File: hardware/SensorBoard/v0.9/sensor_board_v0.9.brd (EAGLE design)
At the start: 52.5 x 43 mm, 43 parts, among them IC1 BMP280, IC2 VREF, J3 USB-MICROB, U1 LMP91000, U10 CCS811, U11 RFM69HW, U2 TSL2561, U3 ATMEGA328P-MU, U7 SHT31, U8 MCP1703/3.3V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

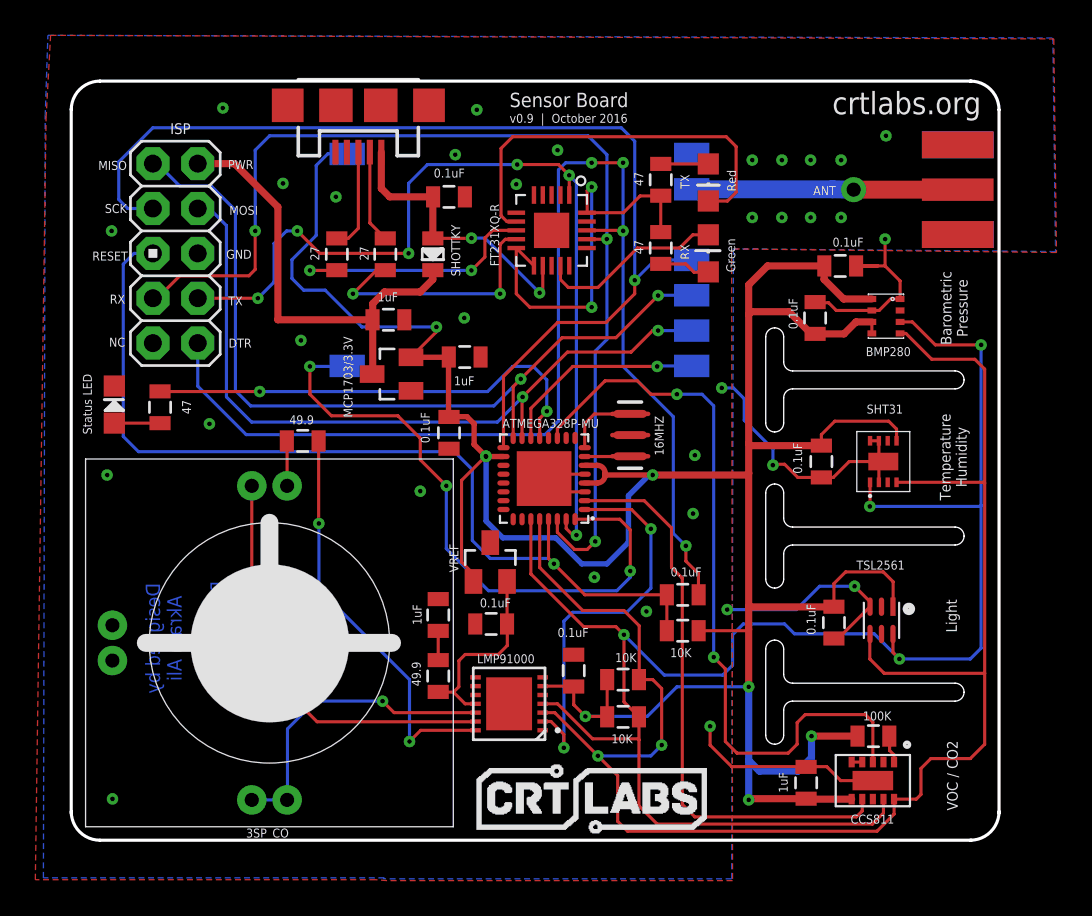
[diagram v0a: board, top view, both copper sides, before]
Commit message: Rearranged several compoents around LMP91000
Rerouted several traces, other touch ups
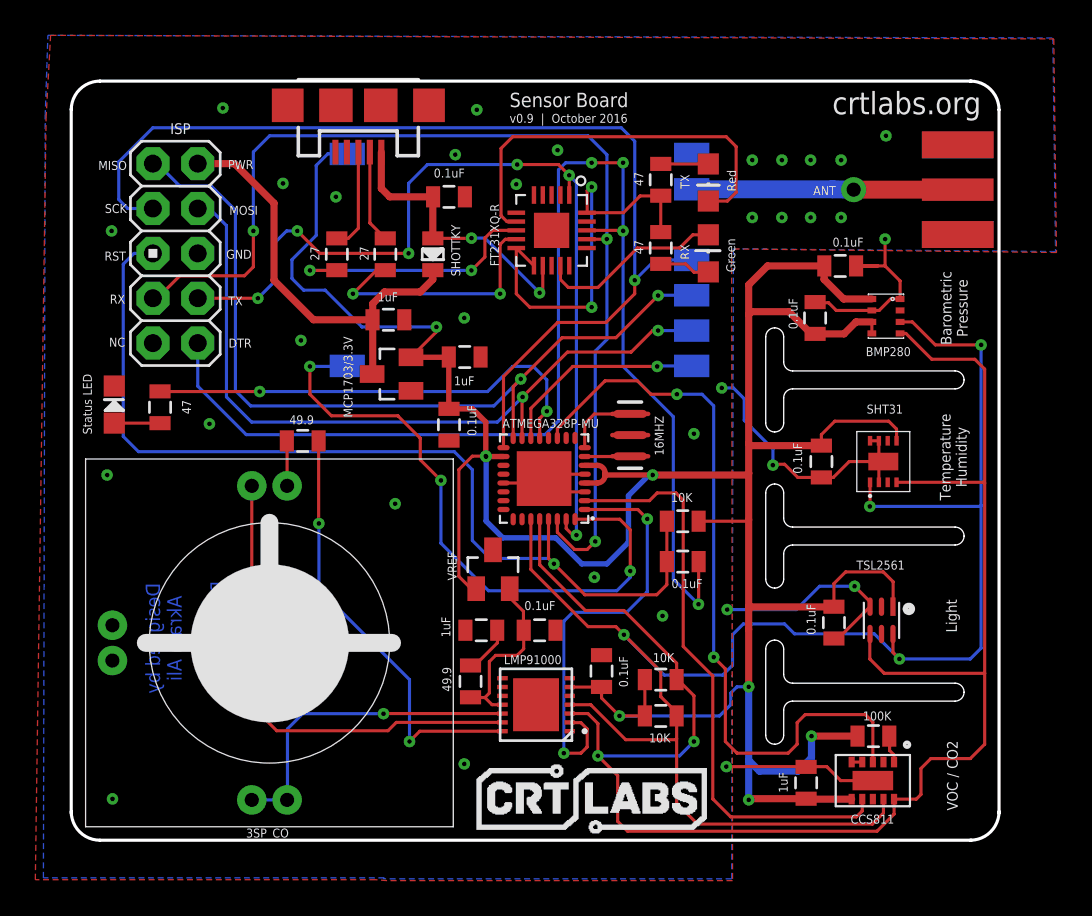
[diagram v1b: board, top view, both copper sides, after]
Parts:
- moved R13 6.20 mm to (38.0, 24.0)
- moved C10 2.77 mm to (29.9, 17.8), turned to 0 degrees
- moved C9 2.59 mm to (26.6, 17.8), turned to 180 degrees
- moved R5 2.13 mm to (36.8, 13.0)
- moved R6 2.13 mm to (36.8, 15.0)
- moved C12 1.88 mm to (38.0, 21.7)
- moved R3 1.85 mm to (26.0, 14.9)
- moved C7 1.58 mm to (33.4, 15.5)
- moved U1 1.52 mm to (29.7, 13.6)
- moved C15 0.46 mm to (24.8, 29.5)
- moved IC2 0.43 mm to (27.3, 21.3)
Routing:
- net RE: track 23.9 -> 27.4 mm
- net DTR: track 70.7 -> 73.6 mm
- net RESET: track 53.2 -> 55.0 mm
- net MENB: track 22.7 -> 24.4 mm
- net N$9: track 23.2 -> 24.7 mm
- net SCL: track 94.2 -> 95.7 mm
- net PWR: track 25.8 -> 24.6 mm
- net N$10: track 1.65 -> 2.77 mm
- net WE: track 17.6 -> 18.6 mm
- net SDA: track 97.5 -> 96.6 mm
- net VREF: track 11.0 -> 10.2 mm
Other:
- board text added: "RST"
- board text removed: "RESET"

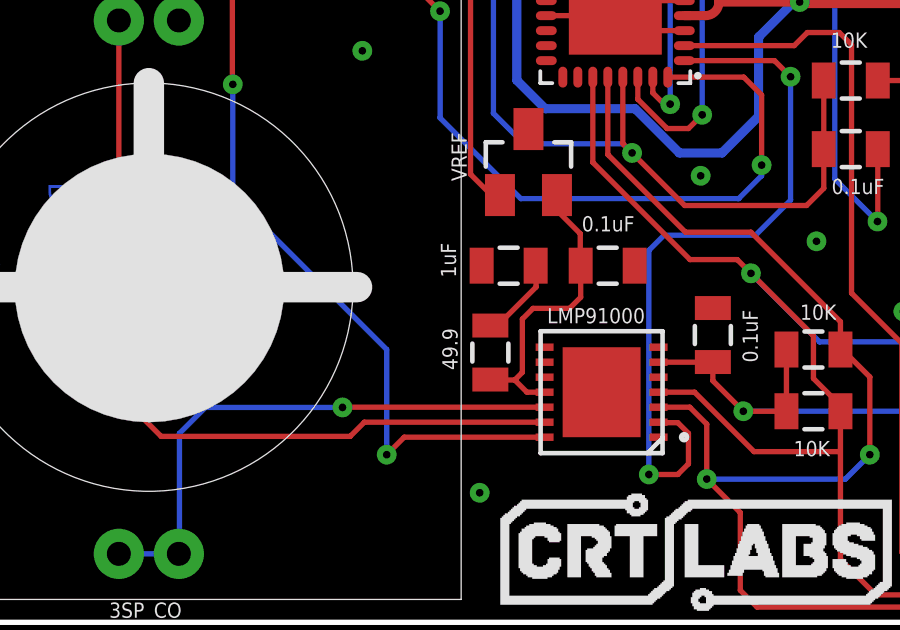
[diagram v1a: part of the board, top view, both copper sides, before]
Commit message: Corrected resistor and capacitor values for voltage ref.
Also added adjusted CCS811 tstop pads
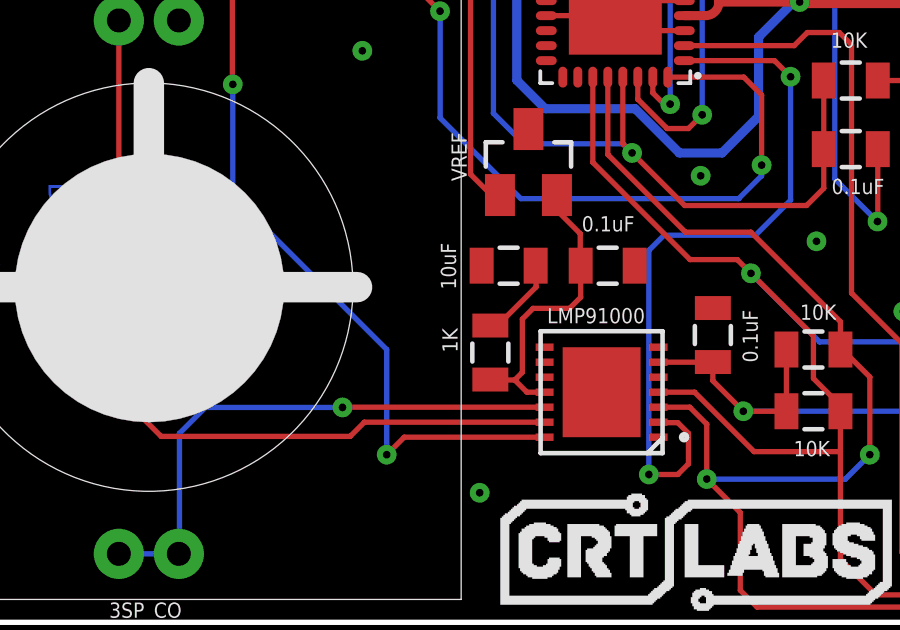
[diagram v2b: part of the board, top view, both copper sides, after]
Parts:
- C9: value 1uF -> 10uF
- R3: value 49.9 -> 1K
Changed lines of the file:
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@@
 <?xml version="1.0" encoding="utf-8"?>
 <!DOCTYPE eagle SYSTEM "eagle.dtd">
-<eagle version="7.6.0">
+<eagle version="7.7.0">
 <drawing>
 <settings>
@@
 <layers>
 <layer number="1" name="Top" color="4" fill="1" visible="yes" active="yes"/>
+<layer number="2" name="Route2" color="1" fill="3" visible="no" active="yes"/>
+<layer number="3" name="Route3" color="4" fill="3" visible="no" active="yes"/>
+<layer number="4" name="Route4" color="1" fill="4" visible="no" active="yes"/>
+<layer number="5" name="Route5" color="4" fill="4" visible="no" active="yes"/>
+<layer number="6" name="Route6" color="1" fill="8" visible="no" active="yes"/>
+<layer number="7" name="Route7" color="4" fill="8" visible="no" active="yes"/>
+<layer number="8" name="Route8" color="1" fill="2" visible="no" active="yes"/>
+<layer number="9" name="Route9" color="4" fill="2" visible="no" active="yes"/>
+<layer number="10" name="Route10" color="1" fill="7" visible="no" active="yes"/>
+<layer number="11" name="Route11" color="4" fill="7" visible="no" active="yes"/>
+<layer number="12" name="Route12" color="1" fill="5" visible="no" active="yes"/>
+<layer number="13" name="Route13" color="4" fill="5" visible="no" active="yes"/>
+<layer number="14" name="Route14" color="1" fill="6" visible="no" active="yes"/>
+<layer number="15" name="Route15" color="4" fill="6" visible="no" active="yes"/>
 <layer number="16" name="Bottom" color="1" fill="1" visible="yes" active="yes"/>
 <layer number="17" name="Pads" color="2" fill="1" visible="yes" active="yes"/>
@@
 <layer number="27" name="tValues" color="7" fill="1" visible="yes" active="yes"/>
 <layer number="28" name="bValues" color="7" fill="1" visible="yes" active="yes"/>
-<layer number="29" name="tStop" color="7" fill="3" visible="no" active="yes"/>
+<layer number="29" name="tStop" color="7" fill="3" visible="yes" active="yes"/>
 <layer number="30" name="bStop" color="7" fill="6" visible="no" active="yes"/>
 <layer number="31" name="tCream" color="7" fill="4" visible="no" active="yes"/>
@@
 <attribute name="VALUE" x="29.0576" y="18.9738" size="0.508" layer="121" font="vector"/>
 </element>
-<element name="R3" library="SparkFun-Passives" package="0805" value="49.9" x="26.0096" y="14.9352" smashed="yes" rot="R270">
+<element name="R3" library="SparkFun-Passives" package="0805" value="1K" x="26.0096" y="14.9352" smashed="yes" rot="R270">
 <attribute name="MF" value="" x="26.0096" y="14.9352" size="1.778" layer="27" rot="R270" display="off"/>
 <attribute name="MPN" value="" x="26.0096" y="14.9352" size="1.778" layer="27" rot="R270" display="off"/>
@@
 <attribute name="VALUE" x="24.4094" y="15.748" size="0.508" layer="121" font="vector" rot="R270"/>
 </element>
-<element name="C9" library="SparkFun-Passives" package="0805" value="1uF" x="26.6192" y="17.8308" smashed="yes" rot="R180">
+<element name="C9" library="SparkFun-Passives" package="0805" value="10uF" x="26.6192" y="17.8308" smashed="yes" rot="R180">
 <attribute name="VALUE" x="24.3586" y="18.5928" size="0.508" layer="121" font="vector" rot="R270"/>
 </element>

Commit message: updated LED descriptions
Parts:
- renumbered LED2 to LED1
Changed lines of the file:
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@@
 </element>
 <element name="C3" library="SparkFun-Passives" package="0805" value="0.1uF" x="46.5836" y="18.2626" smashed="yes" rot="R270">
-<attribute name="MPN" value="CC0603KRX7R7BB104" x="46.5836" y="18.2626" size="1.778" layer="27" rot="R270" display="off"/>
+<attribute name="MPN" value="AC0805KRX7R9BB104" x="46.5836" y="18.2626" size="1.778" layer="27" rot="R270" display="off"/>
 <attribute name="VALUE" x="45.0342" y="19.3294" size="0.508" layer="121" font="vector" rot="R270"/>
 </element>
 <element name="C4" library="SparkFun-Passives" package="0805" value="0.1uF" x="45.8724" y="27.3812" smashed="yes" rot="R270">
-<attribute name="MPN" value="CC0603KRX7R7BB104" x="45.8724" y="27.3812" size="1.778" layer="27" rot="R270" display="off"/>
+<attribute name="MPN" value="AC0805KRX7R9BB104" x="45.8724" y="27.3812" size="1.778" layer="27" rot="R270" display="off"/>
 <attribute name="VALUE" x="44.2722" y="28.448" size="0.508" layer="121" font="vector" rot="R270"/>
 </element>
@@
 <attribute name="VALUE" x="36.9443" y="27.7241" size="0.508" layer="121" font="vector" rot="R90"/>
 </element>
-<element name="LED2" library="adafruit" package="CHIPLED_0805" value="" x="5.842" y="30.607" smashed="yes">
-<attribute name="MPN" value="LTST-C170TBKT" x="5.842" y="30.607" size="1.778" layer="27" display="off"/>
+<element name="LED1" library="adafruit" package="CHIPLED_0805" value="" x="5.842" y="30.607" smashed="yes">
+<attribute name="MPN" value="150080BS75000" x="5.842" y="30.607" size="1.778" layer="27" display="off"/>
 <attribute name="VALUE" x="8.382" y="29.337" size="1.27" layer="27" rot="R90"/>
 </element>
@@
 <element name="C12" library="SparkFun-Passives" package="0805" value="0.1uF" x="38.0238" y="21.717" smashed="yes" rot="R180">
 <attribute name="VALUE" x="39.1414" y="20.7264" size="0.508" layer="121" font="vector" rot="R180"/>
-<attribute name="MPN" value="CC0603KRX7R7BB104" x="38.0238" y="21.717" size="1.778" layer="27" rot="R180" display="off"/>
+<attribute name="MPN" value="AC0805KRX7R9BB104" x="38.0238" y="21.717" size="1.778" layer="27" rot="R180" display="off"/>
 </element>
 <element name="J2" library="SparkFun-Connectors" package="AVR_ICSP" value="" x="9.2964" y="39.1668" smashed="yes">
@@
 </element>
 <element name="RX" library="adafruit" package="CHIPLED_0805" value="Green" x="39.4716" y="39.1668" smashed="yes">
-<attribute name="MPN" value="LTST-C170TBKT" x="39.4716" y="39.1668" size="1.778" layer="27" display="off"/>
+<attribute name="MPN" value="LG R971-KN-1" x="39.4716" y="39.1668" size="1.778" layer="27" display="off"/>
 <attribute name="NAME" x="38.4048" y="38.8112" size="0.508" layer="121" font="vector" rot="R90"/>
 <attribute name="VALUE" x="40.9956" y="38.1" size="0.508" layer="121" font="vector" rot="R90"/>
 </element>
 <element name="TX" library="adafruit" package="CHIPLED_0805" value="Red" x="39.4716" y="43.18" smashed="yes" rot="R180">
-<attribute name="MPN" value="LTST-C170TBKT" x="39.4716" y="43.18" size="1.778" layer="27" rot="R180" display="off"/>
+<attribute name="MPN" value="LH R974-LP-1" x="39.4716" y="43.18" size="1.778" layer="27" rot="R180" display="off"/>
 <attribute name="NAME" x="37.8968" y="43.6372" size="0.508" layer="121" font="vector" rot="R270"/>
 <attribute name="VALUE" x="40.5384" y="43.8912" size="0.508" layer="121" font="vector" rot="R270"/>
@@
 </element>
 <element name="C11" library="SparkFun-Capacitors" package="0805" value="0.1uF" x="24.7904" y="42.3672" smashed="yes">
-<attribute name="MPN" value="CC0603KRX7R7BB104" x="24.7904" y="42.3672" size="1.778" layer="27" display="off"/>
+<attribute name="MPN" value="AC0805KRX7R9BB104" x="24.7904" y="42.3672" size="1.778" layer="27" display="off"/>
 <attribute name="VALUE" x="23.9268" y="43.4594" size="0.508" layer="121" font="vector"/>
 </element>
@@
 <element name="C15" library="SparkFun-Passives" package="0805" value="0.1uF" x="24.7904" y="29.464" smashed="yes" rot="R270">
 <attribute name="VALUE" x="25.8318" y="30.5816" size="0.508" layer="121" font="vector" rot="R270"/>
-<attribute name="MPN" value="CC0603KRX7R7BB104" x="24.7904" y="29.464" size="1.778" layer="27" rot="R270" display="off"/>
+<attribute name="MPN" value="AC0805KRX7R9BB104" x="24.7904" y="29.464" size="1.778" layer="27" rot="R270" display="off"/>
 </element>
 <element name="U10" library="CCS811" package="LGA" value="CCS811" x="46.7868" y="10.668" smashed="yes" rot="R270">
@@
 <element name="C2" library="SparkFun-Passives" package="0805" value="0.1uF" x="45.5168" y="35.5092" smashed="yes" rot="R90">
 <attribute name="VALUE" x="44.0182" y="36.6268" size="0.508" layer="121" font="vector" rot="R270"/>
-<attribute name="MPN" value="CC0603KRX7R7BB104" x="45.5168" y="35.5092" size="1.778" layer="27" rot="R90" display="off"/>
+<attribute name="MPN" value="AC0805KRX7R9BB104" x="45.5168" y="35.5092" size="1.778" layer="27" rot="R90" display="off"/>
 </element>
 <element name="C8" library="SparkFun-Passives" package="0805" value="0.1uF" x="46.9392" y="38.4556" smashed="yes" rot="R180">
 <attribute name="VALUE" x="48.26" y="40.0558" size="0.508" layer="121" font="vector" rot="R180"/>
-<attribute name="MPN" value="CC0603KRX7R7BB104" x="46.9392" y="38.4556" size="1.778" layer="27" rot="R180" display="off"/>
+<attribute name="MPN" value="AC0805KRX7R9BB104" x="46.9392" y="38.4556" size="1.778" layer="27" rot="R180" display="off"/>
 </element>
 <element name="U3" library="ATMEGA328P-MU" package="QFN50P500X500X100-33N" value="ATMEGA328P-MU" x="30.1752" y="26.416" smashed="yes" rot="R180">
@@
 <element name="C7" library="SparkFun-Passives" package="0805" value="0.1uF" x="33.4264" y="15.5194" smashed="yes" rot="R270">
 <attribute name="VALUE" x="34.925" y="14.605" size="0.508" layer="121" font="vector" rot="R90"/>
-<attribute name="MPN" value="CC0603KRX7R7BB104" x="33.4264" y="15.5194" size="1.778" layer="27" rot="R270" display="off"/>
+<attribute name="MPN" value="AC0805KRX7R9BB104" x="33.4264" y="15.5194" size="1.778" layer="27" rot="R270" display="off"/>
 </element>
 <element name="IC2" library="linear" package="SOT23" value="VREF" x="27.2796" y="21.2852" smashed="yes">
 <attribute name="VALUE" x="25.2222" y="20.6502" size="0.508" layer="121" font="vector" rot="R90"/>
-<attribute name="MPN" value="ISL60002DIH320ZCB" x="27.2796" y="21.2852" size="1.778" layer="27" display="off"/>
+<attribute name="MPN" value="ISL60002DIH320Z-TK" x="27.2796" y="21.2852" size="1.778" layer="27" display="off"/>
 </element>
 <element name="C10" library="SparkFun-Passives" package="0805" value="0.1uF" x="29.9212" y="17.8308" smashed="yes">
 <attribute name="VALUE" x="29.0576" y="18.9738" size="0.508" layer="121" font="vector"/>
-<attribute name="MPN" value="CC0603KRX7R7BB104" x="29.9212" y="17.8308" size="1.778" layer="27" display="off"/>
+<attribute name="MPN" value="AC0805KRX7R9BB104" x="29.9212" y="17.8308" size="1.778" layer="27" display="off"/>
 </element>
 <element name="R3" library="SparkFun-Passives" package="0805" value="1K" x="26.0096" y="14.9352" smashed="yes" rot="R270">
@@
 <contactref element="C6" pad="2"/>
 <contactref element="J2" pad="6"/>
-<contactref element="LED2" pad="C"/>
+<contactref element="LED1" pad="C"/>
 <contactref element="C11" pad="2"/>
 <contactref element="J3" pad="MT1"/>
@@
 <signal name="N$3">
 <contactref element="R4" pad="2"/>
-<contactref element="LED2" pad="A"/>
+<contactref element="LED1" pad="A"/>
 <wire x1="8.4328" y1="29.5546" x2="5.842" y2="29.5546" width="0.1778" layer="1"/>
 <wire x1="5.842" y1="29.5546" x2="5.842" y2="29.557" width="0.1778" layer="1"/>
